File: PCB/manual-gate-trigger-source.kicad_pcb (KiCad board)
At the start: 2 copper layers, 108.9 x 110.5 mm, 115 parts, among them J1 PWR, J10 IN1, J11 Conn_01x04, J12 Conn_01x04, J2 OUTa, J3 OUTb, J4 OUTa, J5 OUTb, J6 OUTa, J7 OUTb, J8 OUTa, J9 OUTb, Q2 BC547, Q3 BC547, Q4 BC547, Q5 BC547, Q6 BC547, SW2 ON/ON, SW3 ON/ON, SW4 ON/ON, SW5 ON/ON, SW6 SW_Push, SW7 SW_Push, SW8 SW_Push, U2 LM555xN, U3 LM555xN, U4 LM555xN, U5 LM555xN, U6 LM317L_TO92

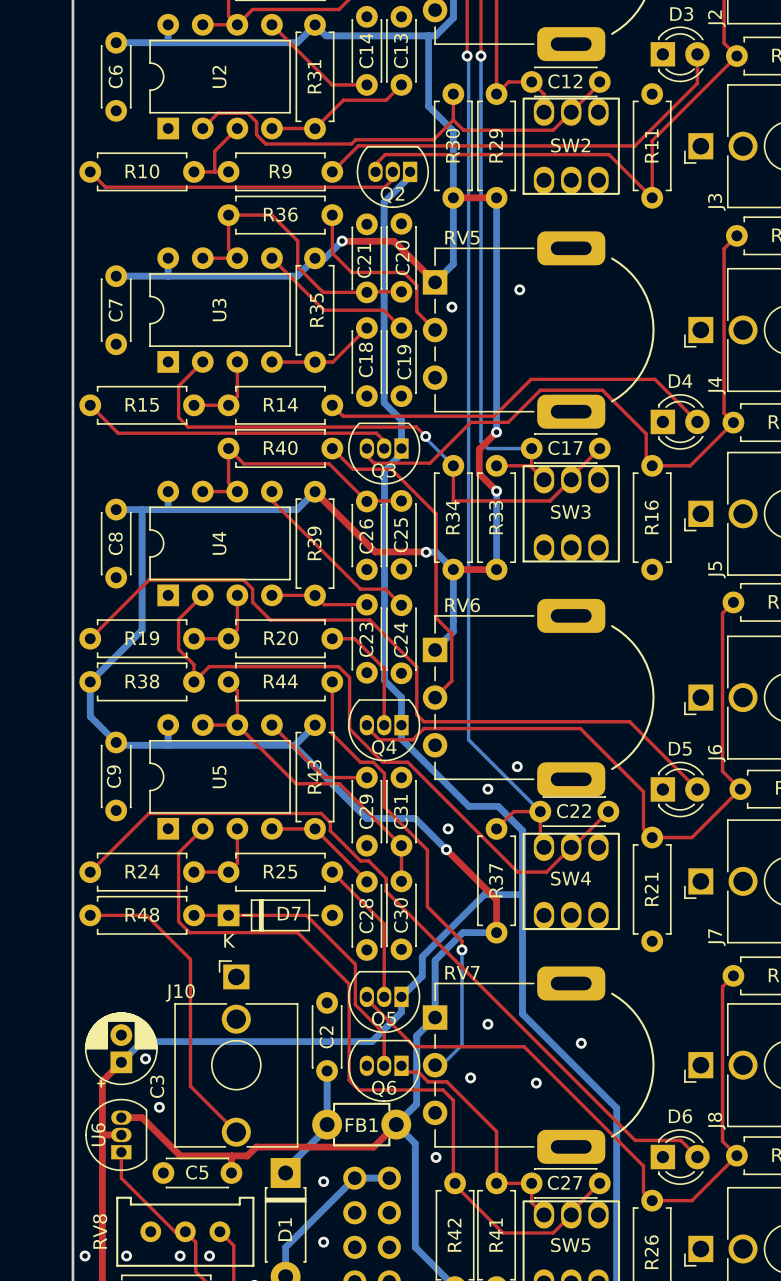
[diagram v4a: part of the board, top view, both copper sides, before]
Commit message: :hammer: Change transistor footprints to hand-solder variant
This fixes #56
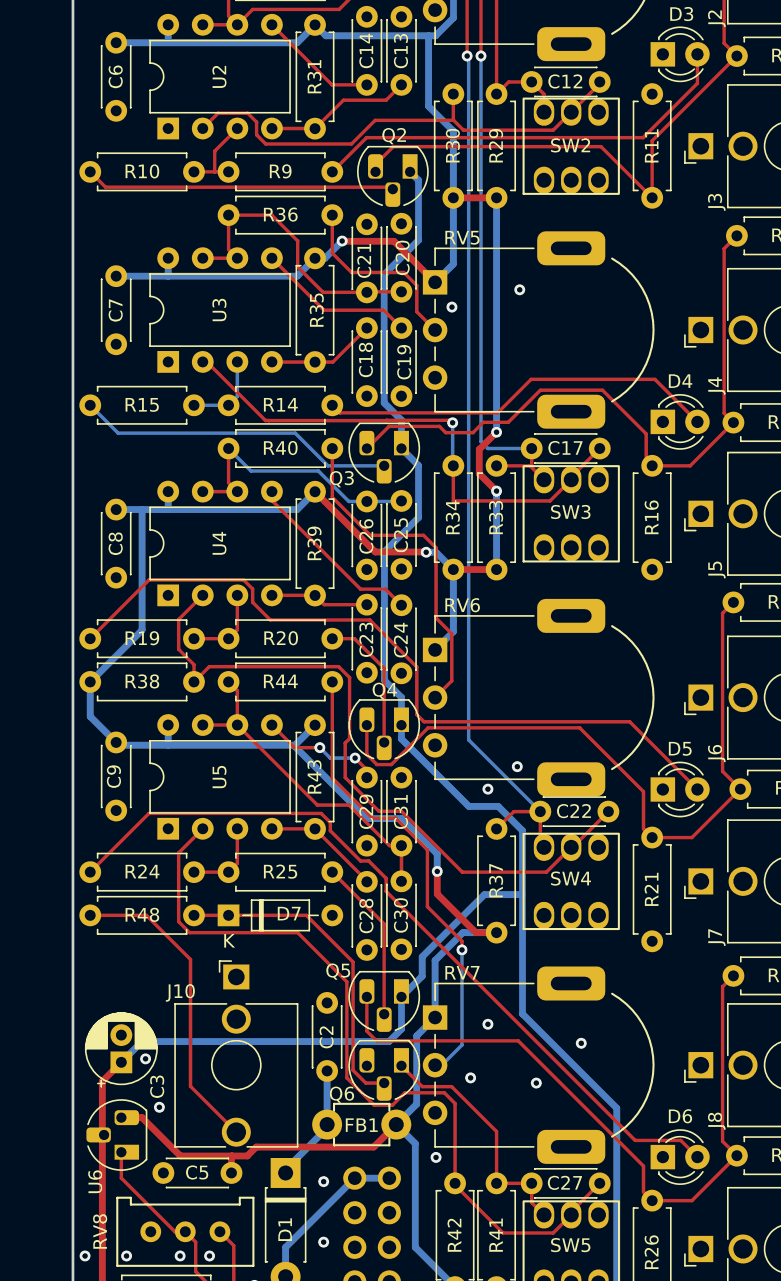
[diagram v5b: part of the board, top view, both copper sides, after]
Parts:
- Q2, Q3, Q4, Q5, Q6, U6: footprint Package_TO_SOT_THT:TO-92_Inline -> Package_TO_SOT_THT:TO-92_HandSolder
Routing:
- net Net-(SW3-A): track 41.6 -> 38.5 mm
- net Net-(Q4-E): track 49.3 -> 52.0 mm
- net Net-(SW4-A): track 48.8 -> 51.3 mm
- net Net-(D7-K): track 21.7 -> 23.7 mm
- net Net-(Q5-E): track 49.9 -> 51.3 mm
- net Net-(Q5-B): track 10.7 -> 12.0 mm
- net Net-(Q4-B): track 8.88 -> 10.2 mm
- net Vdrive: track 150.7 -> 151.7 mm
- net Net-(Q3-E): track 49.0 -> 48.2 mm
- net Net-(Q2-B): track 23.5 -> 22.8 mm
- net Net-(SW5-A): track 57.3 -> 58.0 mm
- net Net-(R40-Pad2): track 24.1 -> 24.7 mm
- net Net-(U5-CV): track 8.57 -> 8.91 mm, vias 0 -> 2
- net GND: vias 24 -> 23

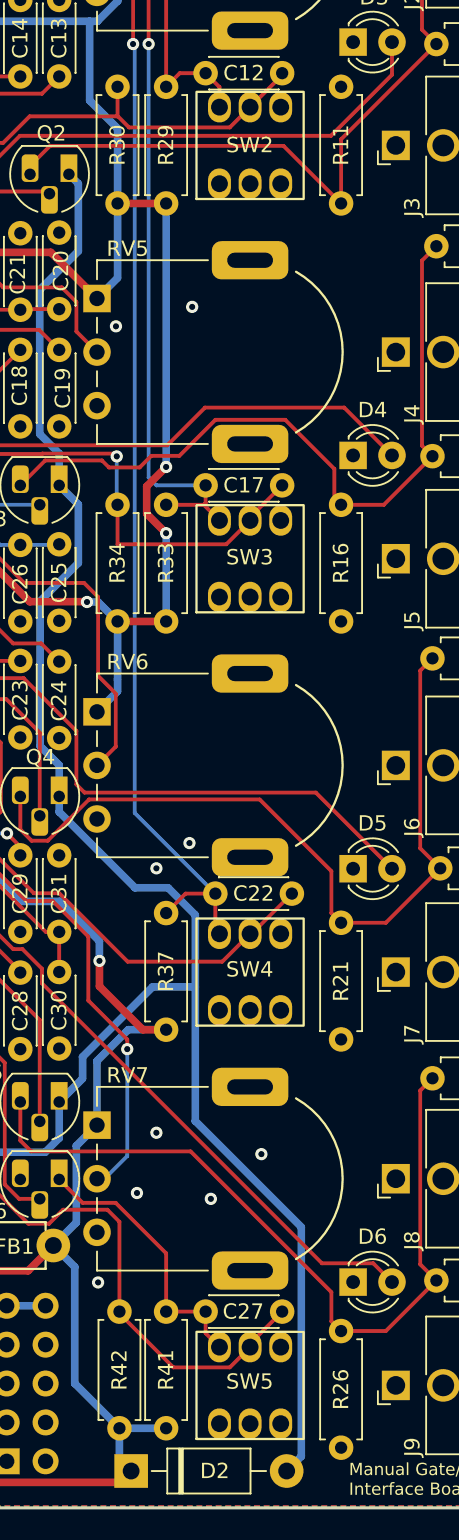
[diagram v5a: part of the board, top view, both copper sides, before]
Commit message: :hammer: Change switch footprints to hybrid version
This allows more flexibility when sourcing the switches

Fixes: #43
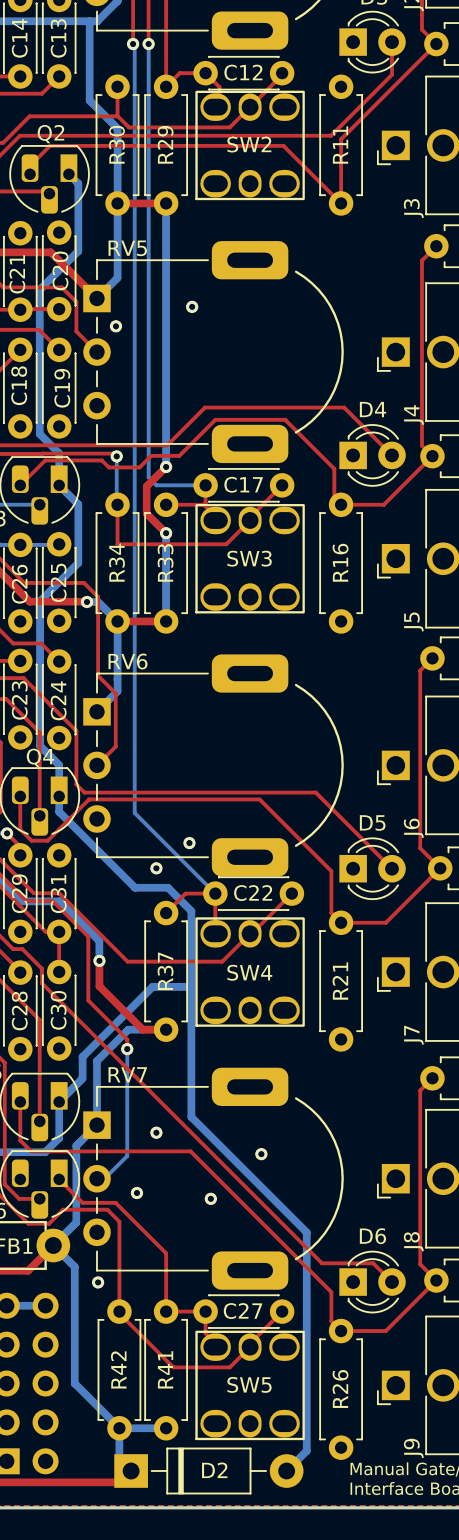
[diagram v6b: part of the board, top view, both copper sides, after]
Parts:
- SW2, SW3, SW4, SW5: footprint moPsy:PB_Hor_7x7_2pole -> moPsy:PB_Hor_7x7_2pole_hybrid

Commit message: :rocket: Update the revision number
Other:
- board text added: "Manual Gate/Trigger Source Interface Board v2"
- board text added: "Manual Gate/Trigger Source Key Board v1/v2"
- board text removed: "Manual Gate/Trigger Source Interface Board v1"
- board text removed: "Manual Gate/Trigger Source Key Board v1"
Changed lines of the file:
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@@
   )
   (paper "A4")
+  (title_block
+    (title "Manual Gate/Trigger Source")
+    (date "2023-05-20")
+    (rev "v2")
+    (company "moPsy")
+  )
   (layers
     (0 "F.Cu" signal)
@@
     (effects (font (size 1 1) (thickness 0.15)) (justify left bottom mirror))
   )
-  (gr_text "Manual Gate/Trigger Source\nKey Board v1" (at 64.21 114.55) (layer "B.SilkS")
+  (gr_text "Manual Gate/Trigger Source\nKey Board v1/v2" (at 64.21 114.55) (layer "B.SilkS")
     (effects (font (size 0.6 0.6) (thickness 0.1) bold) (justify left bottom mirror))
   )
@@
     (effects (font (size 0.6 0.6) (thickness 0.1) bold) (justify right bottom mirror))
   )
-  (gr_text "Manual Gate/Trigger Source\nInterface Board v1" (at 141.553 150.745) (layer "F.SilkS")
+  (gr_text "Manual Gate/Trigger Source\nInterface Board v2" (at 141.553 150.745) (layer "F.SilkS")
     (effects (font (size 0.8 0.8) (thickness 0.15)) (justify left bottom))
   )
